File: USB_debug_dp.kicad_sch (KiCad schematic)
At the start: 0 parts

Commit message: [#82055] Add DP port controller
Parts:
- added C1, C13, C34, C37, C5, C56, C6: C_10u_0402, antmicro-footprints:C_0402_1005Metric, symbol antmicroCapacitors0402:C_10u_0402
- added C10, C11, C12, C14, C140, C141, C143, C144, C15, C16, C2, C3, C35, C38, C39, C54, C55, C7, C9: C_100n_0402, antmicro-footprints:C_0402_1005Metric, symbol antmicroCapacitors0402:C_100n_0402
- added C33, C36: C_4u7_25V_0402, antmicro-footprints:C_0402_1005Metric, symbol antmicroCapacitors0402:C_4u7_25V_0402
- added C41, C42, C43, C44: C_100n_0201, antmicro-footprints:C_0201, symbol antmicroCapacitorsmisc:C_100n_0201
- added C8: C_10u_25V_0603, antmicro-footprints:C_0603_1608Metric, symbol antmicroCapacitors0603:C_10u_25V_0603
- added D1: RB521S30T1G, antmicro-footprints:SOD-523, symbol antmicroDiodesRectifiersSingle:RB521S30T1G
- added D2, D3, D4, D5: LED_G_0603_LTST-C190GKT, antmicro-footprints:LED_0603_1608Metric_G, symbol antmicroLEDIndicationDiscrete:LED_G_0603_LTST-C190GKT
- added J2: USB-C_Amphenol_12401598E4, antmicro-footprints:USB-C_Receptacle_Amphenol_12401598E4, symbol antmicroUSBConnectors:USB-C_Amphenol_12401598E4
- added J3: USB-C_GCT_USB4105-GF-A, antmicro-footprints:USB-C_Receptacle_GCT_USB4105-GF-A, symbol antmicroUSBConnectors:USB-C_GCT_USB4105-GF-A
- added Q1, Q2: PJE138K, antmicro-footprints:SOT-523, symbol antmicroTransistorsFETsMOSFETsSingle:PJE138K
- added R1, R205, R207, R7, R9: R_100k_0402, antmicro-footprints:R_0402_1005Metric, symbol antmicroResistors0402:R_100k_0402
- added R10, R30, R31, R32, R37, R38, R6, R8: R_10k_0402, antmicro-footprints:R_0402_1005Metric, symbol antmicroResistors0402:R_10k_0402
- added R109, R110: R_2M_0402, antmicro-footprints:R_0402_1005Metric, symbol antmicroResistors0402:R_2M_0402
- added R11, R12: R_1k_0402, antmicro-footprints:R_0402_1005Metric, symbol antmicroResistors0402:R_1k_0402
- added R13, R14, R20, R21: R_200R_0402, antmicro-footprints:R_0402_1005Metric, symbol antmicroResistors0402:R_200R_0402
- added R15: R_4x0R_0201_array, antmicro-footprints:R_Array_4x0201_Panasonic_EXB18V, symbol antmicroResistorNetworksArrays:R_4x0R_0201_array
- added R16, R17, R18, R19, R26, R27, R28, R29, R33, R34, R35, R36, R5, R75, R79, R82: R_0R_0402, antmicro-footprints:R_0402_1005Metric, symbol antmicroResistors0402:R_0R_0402
- added R2: R_10M_0402, antmicro-footprints:R_0402_1005Metric, symbol antmicroResistors0402:R_10M_0402
- added R22, R23, R24, R25: R_4k7_0402, antmicro-footprints:R_0402_1005Metric, symbol antmicroResistors0402:R_4k7_0402
- added R39, R40: R_2k2_0402, antmicro-footprints:R_0402_1005Metric, symbol antmicroResistors0402:R_2k2_0402
- added TP1, TP28, TP3, TP30, TP4, TP5, TP6, TP7, TP8: TP_0.75mm_SMD, antmicro-footprints:TP_SMD_0.75mm, symbol antmicroTestPoints:TP_0.75mm_SMD
- added U1: NTS0102_XSON, antmicro-footprints:XSON-8_1x1.95mm_P0.5mm, symbol antmicroLogicTranslatorsLevelShifters:NTS0102_XSON
- added U10: TUSB1046-DCIRNQ, antmicro-footprints:WQFN-40_1EP_6x3mm_Pitch0.4mm_EP4.7x2.7mm, symbol antmicroInterfaceControllers:TUSB1046-DCIRNQ
- added U2: W25Q80DV_USON, antmicro-footprints:USON-8_2x3mm_P0.5mm, symbol antmicroMemory:W25Q80DV_USON
- added U3: TPS65988DHRSHR, antmicro-footprints:IC_TPS65987DDHRSHR, symbol antmicroInterfaceControllers:TPS65988DHRSHR
- added U4: NCP730BMT330_WSON, antmicro-footprints:WSON-6-1EP_2x2mm_P0.65mm, symbol antmicroPMICVoltageRegulatorsLinear:NCP730BMT330_WSON
- added U5: FT230X_QFN, antmicro-footprints:QFN-16-1EP_4x4mm_P0.65mm, symbol antmicroInterfaceControllers:FT230X_QFN
- added U6, U7: AP22615A_TSOT26, antmicro-footprints:TSOT23-6, symbol antmicroPMICPowerDistributionSwitchesLoadDrivers:AP22615A_TSOT26
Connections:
- new net: TP28.1, U10.29 (CAD_SNK/RSVD1)
- new net: C43.1, J2.B2 (TX_{2}+)
- new net: D2.2 (A), R13.1
- new net: C10.1, R30.2, U5.9 (~{RESET})
- new net: D5.2 (A), R21.2
- new net: D4.2 (A), R20.2
- new net: R34.2, R37.2, U6.4 (EN)
- new net: Q2.1 (G), R2.2
- new net: J2.A4 (VBUS), J2.A9 (VBUS), J2.B4 (VBUS), J2.B9 (VBUS), U3.13 (VBUS1), U7.1 (OUT)
- new net: R36.2, R38.2, U7.4 (EN)
- new net: R40.2, U7.5 (ISET)
- new net: TP8.1, U3.30 (GPIO3/HPD1)
- new net: U3.15 (DRAIN1), U3.19 (DRAIN1), U3.58 (DRAIN1), U3.8 (DRAIN1)
- new net: J2.A5 (CC_{1}), U3.24 (C1_CC1)
- new net: J2.B5 (CC_{2}), U3.26 (C1_CC2)
- new net: R39.2, U6.5 (ISET)
- new net: C41.1, J2.A2 (TX_{1}+)
- new net: C42.1, J2.A3 (TX_{1}-)
- new net: C44.1, J2.B3 (TX_{2}-)
- new net: R29.2, U5.4 (~{CTS})
- new net: J3.A4 (VBUS), J3.A9 (VBUS), J3.B4 (VBUS), J3.B9 (VBUS), U3.3 (VBUS2), U6.1 (OUT)
- new net: J3.A5 (CC_{1}), U3.45 (C2_CC1)
- new net: J3.B5 (CC_{2}), U3.47 (C2_CC2)
- new net: R28.2, U5.16 (~{RTS})
- new net: R27.2, U5.2 (RXD)
- new net: R26.2, U5.15 (TXD)
- new net: D3.2 (A), R14.1
- new net: U3.52 (DRAIN2), U3.56 (DRAIN2), U3.57 (DRAIN2), U3.7 (DRAIN2)
- new net +3V3: C1.2, C2.1, C38.1, C39.1, C54.1, C55.1, C56.2, R207.2, R22.1, R23.1, R24.1, R25.1, R31.2, R32.2, U10.1 (VCC), U10.20 (VCC), U10.28 (VCC), U10.6 (VCC), U3.5 (VIN_3V3)
- new net +5V: C15.1, C34.1, C35.1, C37.1, R33.2, R35.2, U3.25 (PP1_CABLE), U3.46 (PP2_CABLE), U6.6 (IN), U7.6 (IN)
- new net DEBUG_RXD: R26.1
- new net DEBUG_TXD: R27.1
- new net DP1_AUX_N: R207.1, U10.25 (AUX_N)
- new net DP1_AUX_P: R205.1, U10.24 (AUX_P)
- new net DP1_TXD0_N: U10.10 (DP0_N)
- new net DP1_TXD0_P: U10.9 (DP0_P)
- new net DP1_TXD1_N: U10.13 (DP1_N)
- new net DP1_TXD1_P: U10.12 (DP1_P)
- new net DP1_TXD2_N: U10.16 (DP2_N)
- new net DP1_TXD2_P: U10.15 (DP2_P)
- new net DP1_TXD3_N: U10.19 (DP3_N)
- new net DP1_TXD3_P: U10.18 (DP3_P)
- new net EEPROM_PWR: C9.2, D1.1 (C), R10.2, U2.3 (~{WP}/IO2), U2.7 (~{HOLD}/IO3), U2.8 (VCC)
- new net FTDI_3V3: C11.1, C12.1, C13.2, C3.1, C7.1, R1.2, R11.2, R12.2, R13.2, R14.2, R30.1, U1.3 (VCC_{A}), U1.7 (VCC_{B}), U4.1 (V_{OUT}), U5.1 (V_{CCIO}), U5.10 (V_{CC}), U5.8 (3V3_{OUT})
- new net FTDI_CBUS0/SDA: R12.1, U1.5 (A_{1}), U5.12 (CBUS0)
- new net FTDI_CBUS3/SCL: R11.1, U1.4 (A_{2}), U5.14 (CBUS3)
- new net FTDI_CBUS_EN: Q1.3 (D), Q2.3 (D), R1.1, U1.6 (OE)
- new net FTDI_LED_RX: D3.1 (C), Q1.1 (G), U5.11 (CBUS1)
- new net FTDI_LED_TX: D2.1 (C), U5.5 (CBUS2)
- new net GND: C1.1, C10.2, C11.2, C12.2, C13.1, C14.2, C15.2, C16.2, C2.2, C3.2, C33.2, C34.2, C35.2, C36.2, C37.2, C38.2, C39.2, C5.1, C54.2, C55.2, C56.1, C6.1, C7.2, C8.2, C9.1, D4.1 (C), D5.1 (C), J2.A1 (GND), J2.A12 (GND), J2.B1 (GND), J2.B12 (GND), J2.SH, J3.A1 (GND), J3.A12 (GND), J3.B1 (GND), J3.B12 (GND), J3.SH, Q1.2 (S), Q2.2 (S), R109.2, R110.2, R2.1, R205.2, R37.1, R38.1, R39.1, R40.1, R5.1, R7.1, R9.1, U1.2 (GND), U2.4 (VSS), U3.20 (GND), U3.51 (GND), U3.59 (GND_EP), U4.3 (GND), U4.5 (PG), U4.7 (GND), U5.13 (GND), U5.17 (GND), U5.3 (GND), U6.2 (GND), U7.2 (GND)
- new net GPIO010: R17.1
- new net HPDIN: R75.2, U10.32 (HPDIN/RSVD2)
- new net PDC_ADCIN1: R6.2, R7.2, U3.6 (ADCIN1)
- new net PDC_ADCIN2: R8.2, R9.2, U3.10 (ADCIN2)
- new net PDC_CTL0: R15.2 (R2.1), U3.17 (GPIO1)
- new net PDC_CTL1: R15.1 (R1.1), U3.18 (GPIO2)
- new net PDC_FLIP: R15.3 (R3.1), U3.16 (GPIO0)
- new net PDC_GPIO14: R20.1, U3.42 (GPIO14/PWM1)
- new net PDC_GPIO15: R21.1, U3.43 (GPIO15/PWM2)
- new net PDC_HPD2: R16.2, U3.31 (GPIO4/HPD2)
- new net PDC_I2C1_IRQn: R17.2, U3.29 (~{I2C1_IRQ})
- new net PDC_I2C1_SCL: R18.2, R23.2, U3.27 (I2C1_SCL)
- new net PDC_I2C1_SDA: R19.2, R22.2, U3.28 (I2C1_SDA)
- new net PDC_I2C2_IRQn: TP1.1, U3.34 (~{I2C2_IRQ})
- new net PDC_I2C2_SCL: R25.2, TP3.1, U3.32 (I2C2_SCL)
- new net PDC_I2C2_SDA: R24.2, TP4.1, U3.33 (I2C2_SDA)
- new net PDC_I2C3_SCL: TP5.1, U3.21 (I2C3_SCL/GPIO5)
- new net PDC_I2C3_SDA: TP6.1, U3.22 (I2C3_SDA/GPIO6)
- new net PDC_LDO_1V8: C5.2, U3.35 (LDO_1V8)
- new net PDC_LDO_3V3: C6.2, D1.2 (A), R6.1, R8.1, U3.9 (LDO_3V3)
- new net PDC_MISO: R10.1, U2.2 (SO/IO1), U3.36 (SPI_POCI/GPIO8)
- new net PDC_MOSI: U2.5 (SI/IO0), U3.37 (SPI_PICO/GPIO9)
- new net PDC_RESET: R5.2, U3.44 (HRESET)
- new net PDC_SCLK: U2.6 (SCLK), U3.38 (SPI_CLK/GPIO10)
- new net PWR_SOFT: R28.1
- new net SYS_CLK: R18.1, U1.1 (B_{2})
- new net SYS_SCL: R82.2
- new net SYS_SDA: R19.1, R79.2, U1.8 (B_{1})
- new net USBC0_5V_PEN: R35.1, R36.1, U3.48 (GPIO16/PP_EXT1)
- new net USBC0_CTL0: R15.7 (R2.2), R79.1, U10.22 (CTL0/SDA)
- new net USBC0_CTL1: R15.8 (R1.2), U10.23 (CTL1/HPDIN)
- new net USBC0_DPEQ0: U10.14 (DPEQ0/A1)
- new net USBC0_DPEQ1: U10.2 (DPEQ1)
- new net USBC0_EQ0: U10.38 (EQ0)
- new net USBC0_EQ1: U10.35 (EQ1)
- new net USBC0_FLG: R32.1, U7.3 (FLG)
- new net USBC0_FLIP: R15.6 (R3.2), R82.1, U10.21 (FLIP/SCL)
- new net USBC0_I2C_EN: U10.17 (I2C_EN)
- new net USBC0_RX1_N: J2.B10 (RX_{1}-), U10.31 (RX1_N)
- new net USBC0_RX1_P: J2.B11 (RX_{1}+), U10.30 (RX1_P)
- new net USBC0_RX2_N: J2.A10 (RX_{2}-), U10.39 (RX2_N)
- new net USBC0_RX2_P: J2.A11 (RX_{2}+), U10.40 (RX2_P)
- new net USBC0_SBU_N: J2.A8 (SBU_{1}), R109.1, U10.27 (SBU1)
- new net USBC0_SBU_P: J2.B8 (SBU_{2}), R110.1, U10.26 (SBU2)
- new net USBC0_SSEQ0: U10.11 (SSEQ0/A0)
- new net USBC0_SSEQ1: U10.3 (SSEQ1)
- new net USBC0_TX1_N: C42.2, U10.34 (TX1_N)
- new net USBC0_TX1_P: C41.2, U10.33 (TX1_P)
- new net USBC0_TX2_N: C44.2, U10.36 (TX2_N)
- new net USBC0_TX2_P: C43.2, U10.37 (TX2_P)
- new net USBC1_5V_PEN: R33.1, R34.1, U3.49 (GPIO17/PP_EXT2)
- new net USBC1_FLG: R31.1, U6.3 (FLG)
- new net USBC3_VBUS: C8.1, U4.4 (EN), U4.6 (V_{IN})
- new net USBC_HPD: R16.1, R75.1, TP30.1
- new net USBPD0_HV: C16.1, C36.1, U3.11 (PP_HV1)
- new net USBPD1_HV: C14.1, C33.1, U3.1 (PP_HV2)
- new net USBSS0_RX_C_N: C140.2, U10.4 (SSRX_N)
- new net USBSS0_RX_C_P: C143.2, U10.5 (SSRX_P)
- new net USBSS0_RX_N: C143.1
- new net USBSS0_RX_P: C140.1
- new net USBSS0_TX_C_N: C141.2, U10.7 (SSTX_N)
- new net USBSS0_TX_C_P: C144.2, U10.8 (SSTX_P)
- new net USBSS0_TX_N: C144.1
- new net USBSS0_TX_P: C141.1
- new net USB_FTDI_N: J3.A7 (D_{A}-), J3.B7 (D_{B}-), U5.7 (D-)
- new net USB_FTDI_P: J3.A6 (D_{A}+), J3.B6 (D_{B}+), U5.6 (D+)
- new net ~{PDC_CS}: U2.1 (~{CS}), U3.39 (~{SPI_CS}/GPIO11)
- new net ~{PDC_I2C3_IRQ}: TP7.1, U3.23 (~{I2C3_IRQ}/GPIO7)
- no-connect marks 0 -> 14
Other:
- note added: "4 LANE DP"
- note added: "CONFIGURATION"
- note added: "CTL0"
- note added: "CTL1"
- note added: "H"
- note added: "I_{LIM}(A) = 6800/R_{LIM} = 3.09"
- note added: "L"
- note added: "POWER DOWN"
- note added: "RX"
- note added: "TX"
- note added: "USB + 2 LANE DP"
- note added: "USB ONLY"
- note added: "USB PORT 0"
- note added: "USB PORT 1"

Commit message: [#82055] Add DP eq connections, cleanup schematic
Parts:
- removed C35: C_100n_0402, antmicro-footprints:C_0402_1005Metric, symbol antmicroCapacitors0402:C_100n_0402
- removed D1: RB521S30T1G, antmicro-footprints:SOD-523, symbol antmicroDiodesRectifiersSingle:RB521S30T1G
- removed J3: USB-C_GCT_USB4105-GF-A, antmicro-footprints:USB-C_Receptacle_GCT_USB4105-GF-A, symbol antmicroUSBConnectors:USB-C_GCT_USB4105-GF-A
- removed Q1: PJE138K, antmicro-footprints:SOT-523, symbol antmicroTransistorsFETsMOSFETsSingle:PJE138K
- removed R1, R7, R9: R_100k_0402, antmicro-footprints:R_0402_1005Metric, symbol antmicroResistors0402:R_100k_0402
- removed R10: R_10k_0402, antmicro-footprints:R_0402_1005Metric, symbol antmicroResistors0402:R_10k_0402
- removed R12: R_1k_0402, antmicro-footprints:R_0402_1005Metric, symbol antmicroResistors0402:R_1k_0402
- removed R17, R19, R5, R75, R82: R_0R_0402, antmicro-footprints:R_0402_1005Metric, symbol antmicroResistors0402:R_0R_0402
- removed R22, R25: R_4k7_0402, antmicro-footprints:R_0402_1005Metric, symbol antmicroResistors0402:R_4k7_0402
- removed TP1: TP_0.75mm_SMD, antmicro-footprints:TP_SMD_0.75mm, symbol antmicroTestPoints:TP_0.75mm_SMD
- removed U3: TPS65988DHRSHR, antmicro-footprints:IC_TPS65987DDHRSHR, symbol antmicroInterfaceControllers:TPS65988DHRSHR
- added C145, C146: C_47p_0402, antmicro-footprints:C_0402_1005Metric, symbol antmicroCapacitors0402:C_47p_0402
- added C147: C_1u_25V_0402, antmicro-footprints:C_0402_1005Metric, symbol antmicroCapacitors0402:C_1u_25V_0402
- added C40, C93: C_100n_0402, antmicro-footprints:C_0402_1005Metric, symbol antmicroCapacitors0402:C_100n_0402
- added D19: DF2S30FS_SOD, antmicro-footprints:SOD-923, symbol antmicroTVSDiodes:DF2S30FS_SOD
- added D20: LED_G_0603_LTST-C190GKT, antmicro-footprints:LED_0603_1608Metric_G, symbol antmicroLEDIndicationDiscrete:LED_G_0603_LTST-C190GKT
- added D6: RB521S30T1G, antmicro-footprints:SOD-523, symbol antmicroDiodesRectifiersSingle:RB521S30T1G
- added J4: USB-C_GCT_USB4105-GF-A, antmicro-footprints:USB-C_Receptacle_GCT_USB4105-GF-A, symbol antmicroUSBConnectors:USB-C_GCT_USB4105-GF-A
- added Q3: PJE138K, antmicro-footprints:SOT-523, symbol antmicroTransistorsFETsMOSFETsSingle:PJE138K
- added R100, R101, R102, R103, R104, R105, R106, R107, R108, R111, R113, R63, R67, R68, R70: R_1k_0402, antmicro-footprints:R_0402_1005Metric, symbol antmicroResistors0402:R_1k_0402
- added R117, R127: R_27R_0402, antmicro-footprints:R_0402_1005Metric, symbol antmicroResistors0402:R_27R_0402
- added R41, R56, R58, R61, R65: R_0R_0402, antmicro-footprints:R_0402_1005Metric, symbol antmicroResistors0402:R_0R_0402
- added R42, R43, R54: R_100k_0402, antmicro-footprints:R_0402_1005Metric, symbol antmicroResistors0402:R_100k_0402
- added R48: R_10k_0402, antmicro-footprints:R_0402_1005Metric, symbol antmicroResistors0402:R_10k_0402
- added R50, R52, R71: R_4k7_0402, antmicro-footprints:R_0402_1005Metric, symbol antmicroResistors0402:R_4k7_0402
- added TP9: TP_0.75mm_SMD, antmicro-footprints:TP_SMD_0.75mm, symbol antmicroTestPoints:TP_0.75mm_SMD
- added U17, U18, U19, U20: TPD4E05U06QDQARQ1, antmicro-footprints:USON-10_2.5x1mm_P0.5mm, symbol antmicroTVSDiodes:TPD4E05U06QDQARQ1
- added U8: TPS65988DHRSHR, antmicro-footprints:IC_TPS65987DDHRSHR, symbol antmicroInterfaceControllers:TPS65988DHRSHR
- renumbered C1 to C60, C2 to C61, C5 to C62, C6 to C63, C9 to C64, C8 to C65, C56 to C66, C38 to C67, C39 to C68, C143 to C69, C144 to C70, C140 to C71, C141 to C72, C54 to C73, C55 to C74, C11 to C75, C12 to C76, C13 to C77, C3 to C78, C7 to C79, C10 to C80, C41 to C81, C43 to C82, C16 to C83, C14 to C84, C42 to C86, C44 to C87, C15 to C88, C36 to C89, C37 to C90, C33 to C91, C34 to C92, D4 to D15, D5 to D16, D2 to D17, D3 to D18, J2 to J4, Q2 to Q15, R6 to R56, R8 to R58, R15 to R61, R16 to R63, R18 to R65, R20 to R67, R21 to R68, R23 to R70, R24 to R71, R2 to R73, R11 to R74, R207 to R76, R205 to R77, R13 to R78, R14 to R80, R79 to R81, R26 to R83, R27 to R84, R28 to R85, R29 to R86, R32 to R87, R31 to R88, R30 to R89, R35 to R90, R33 to R91, R36 to R92, R34 to R93, R38 to R94, R37 to R95, R40 to R96, R39 to R97, R109 to R98, R110 to R99, TP4 to TP10, TP5 to TP11, TP6 to TP12, TP7 to TP13, TP8 to TP14, TP30 to TP15, TP28 to TP16, TP3 to TP9, U4 to U11, U1 to U12, U10 to U13, U5 to U14, U7 to U15, U6 to U16, U2 to U9
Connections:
- net +3V3: now also R100.2, R102.2, R104.2, R106.2, R108.2, R50.1, R52.1, R68.2, R70.2, U8.5 (VIN_3V3)
- net +5V: now also C40.1, U8.25 (PP1_CABLE), U8.46 (PP2_CABLE)
- net EEPROM_PWR: now also D6.1 (C), R48.2
- net FTDI_3V3: now also R54.2, R63.2
- net FTDI_CBUS0/SDA: now also R63.1
- net FTDI_CBUS_EN: now also Q3.3 (D), R54.1
- net FTDI_LED_RX: now also Q3.1 (G)
- net GND: now also U13.41 (GND), C145.1, C146.2, C147.2, C40.2, C93.2, D19.2 (A), D20.1 (C), J4.A1 (GND), J4.A12 (GND), J4.B1 (GND), J4.B12 (GND), J4.SH, Q3.2 (S), R101.2, R103.2, R105.2, R107.2, R111.2, R113.2, R41.1, R42.1, R43.1, R67.2, U17.3, U17.8, U18.3, U18.8, U19.3, U19.8, U20.3, U20.8, U8.20 (GND), U8.51 (GND), U8.59 (GND_EP)
- net GPIO010: now also R56.1
- net HPDIN: now also R61.2
- net PDC_ADCIN1: now also R42.2, U8.6 (ADCIN1)
- net PDC_ADCIN2: now also R43.2, U8.10 (ADCIN2)
- net PDC_CTL0: now also U8.17 (GPIO1)
- net PDC_CTL1: now also U8.18 (GPIO2)
- net PDC_FLIP: now also U8.16 (GPIO0)
- net PDC_GPIO14: now also U8.42 (GPIO14/PWM1)
- net PDC_GPIO15: now also U8.43 (GPIO15/PWM2)
- net PDC_HPD2: now also U8.31 (GPIO4/HPD2)
- net PDC_I2C1_IRQn: now also R56.2, U8.29 (~{I2C1_IRQ})
- net PDC_I2C1_SCL: now also R50.2, U8.27 (I2C1_SCL); no longer R70.2
- net PDC_I2C1_SDA: now also R70.2, R58.2, U8.28 (I2C1_SDA)
- net PDC_I2C2_IRQn: now also TP9.1, U8.34 (~{I2C2_IRQ})
- net PDC_I2C2_SCL: now also R71.2, U8.32 (I2C2_SCL)
- net PDC_I2C2_SDA: now also R52.2, U8.33 (I2C2_SDA); no longer R71.2
- net PDC_I2C3_SCL: now also U8.21 (I2C3_SCL/GPIO5)
- net PDC_I2C3_SDA: now also U8.22 (I2C3_SDA/GPIO6)
- net PDC_LDO_1V8: now also U8.35 (LDO_1V8)
- net PDC_LDO_3V3: now also D6.2 (A), U8.9 (LDO_3V3)
- net PDC_MISO: now also R48.1, U8.36 (SPI_POCI/GPIO8)
- net PDC_MOSI: now also U8.37 (SPI_PICO/GPIO9)
- net PDC_RESET: now also R41.2, U8.44 (HRESET)
- net PDC_SCLK: now also U8.38 (SPI_CLK/GPIO10)
- net SYS_SCL: now also R65.2
- net SYS_SDA: now also R58.1
- net USBC0_5V_PEN: now also U8.48 (GPIO16/PP_EXT1)
- net USBC0_FLIP: now also R65.1
- net USBC0_RX1_N: now also U20.5, U20.6
- net USBC0_RX1_P: now also U20.4, U20.7
- net USBC0_RX2_N: now also U19.5, U19.6
- net USBC0_RX2_P: now also U19.4, U19.7
- net USBC0_SBU_N: now also U18.4, U18.7
- net USBC0_SBU_P: now also U18.5, U18.6
- net USBC1_5V_PEN: now also U8.49 (GPIO17/PP_EXT2)
- net USBC_HPD: now also R61.1
- net USBPD0_HV: now also U8.11 (PP_HV1)
- net USBPD1_HV: now also U8.1 (PP_HV2)
- net USB_FTDI_N: now also R117.1
- net USB_FTDI_P: now also R127.1
- net ~{PDC_CS}: now also U8.39 (~{SPI_CS}/GPIO11)
- net ~{PDC_I2C3_IRQ}: now also U8.23 (~{I2C3_IRQ}/GPIO7)
- net at C82.1, J4.B2 (TX_{2}+): now also U18.1, U18.10
- net ~{PERIPHERAL_RESET}: now reaches Q15.1 (G), R73.2
- net at J4.A4 (VBUS), J4.A9 (VBUS), J4.B4 (VBUS)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: now also U8.13 (VBUS1)
- net at TP14.1: now also U8.30 (GPIO3/HPD1)
- net at J4.A5 (CC_{1}): now also U17.5, U17.6, U8.24 (C1_CC1)
- net at J4.B5 (CC_{2}): now also U17.4, U17.7, U8.26 (C1_CC2)
- net at C81.1, J4.A2 (TX_{1}+): now also U19.1, U19.10
- net at C86.1, J4.A3 (TX_{1}-): now also U19.2, U19.9
- net USB0_D+: now reaches J4.A6 (D_{A}+)
- net USB0_D+: now also J4.B6 (D_{B}+), U17.2, U17.9
- net USB0_D-: now reaches J4.A7 (D_{A}-)
- net USB0_D-: now also J4.B7 (D_{B}-), U17.1, U17.10
- net at C87.1, J4.B3 (TX_{2}-): now also U18.2, U18.9
- net at U16.1 (OUT): now also C147.1, C93.1, D19.1 (C), J4.A4 (VBUS), J4.A9 (VBUS), J4.B4 (VBUS), J4.B9 (VBUS), R71.1, U8.3 (VBUS2)
- net USBC0_DPEQ0: no longer names the net of U13.14 (DPEQ0/A1)
- net USBC0_DPEQ0: now also R106.1, R107.1
- net USBC0_DPEQ1: no longer names the net of U13.2 (DPEQ1)
- net USBC0_DPEQ1: now also R108.1, R67.1
- net USBC0_EQ0: no longer names the net of U13.38 (EQ0)
- net USBC0_EQ0: now also R111.1, R68.1
- net USBC0_EQ1: no longer names the net of U13.35 (EQ1)
- net USBC0_EQ1: now also R113.1, R70.1
- net USBC0_I2C_EN: no longer names the net of U13.17 (I2C_EN)
- net USBC0_I2C_EN: now also R100.1, R101.1
- net USBC0_SSEQ0: no longer names the net of U13.11 (SSEQ0/A0)
- net USBC0_SSEQ0: now also R102.1, R103.1
- net USBC0_SSEQ1: no longer names the net of U13.3 (SSEQ1)
- net USBC0_SSEQ1: now also R104.1, R105.1
- new net: C145.2, J4.A7 (D_{A}-), J4.B7 (D_{B}-), R117.2
- new net: C146.1, J4.A6 (D_{A}+), J4.B6 (D_{B}+), R127.2
- new net: D20.2 (A), R71.2
- new net: U20.1, U20.10
- new net: U20.2, U20.9
- new net: U8.15 (DRAIN1), U8.19 (DRAIN1), U8.58 (DRAIN1), U8.8 (DRAIN1)
- new net: J4.A5 (CC_{1}), U8.45 (C2_CC1)
- new net: J4.B5 (CC_{2}), U8.47 (C2_CC2)
- new net: U8.52 (DRAIN2), U8.56 (DRAIN2), U8.57 (DRAIN2), U8.7 (DRAIN2)
- no-connect marks 14 -> 16
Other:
- moved on the sheet: C60, C61, C62, C63, C64, C65, C66, C67, C68, C69, C70, C71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

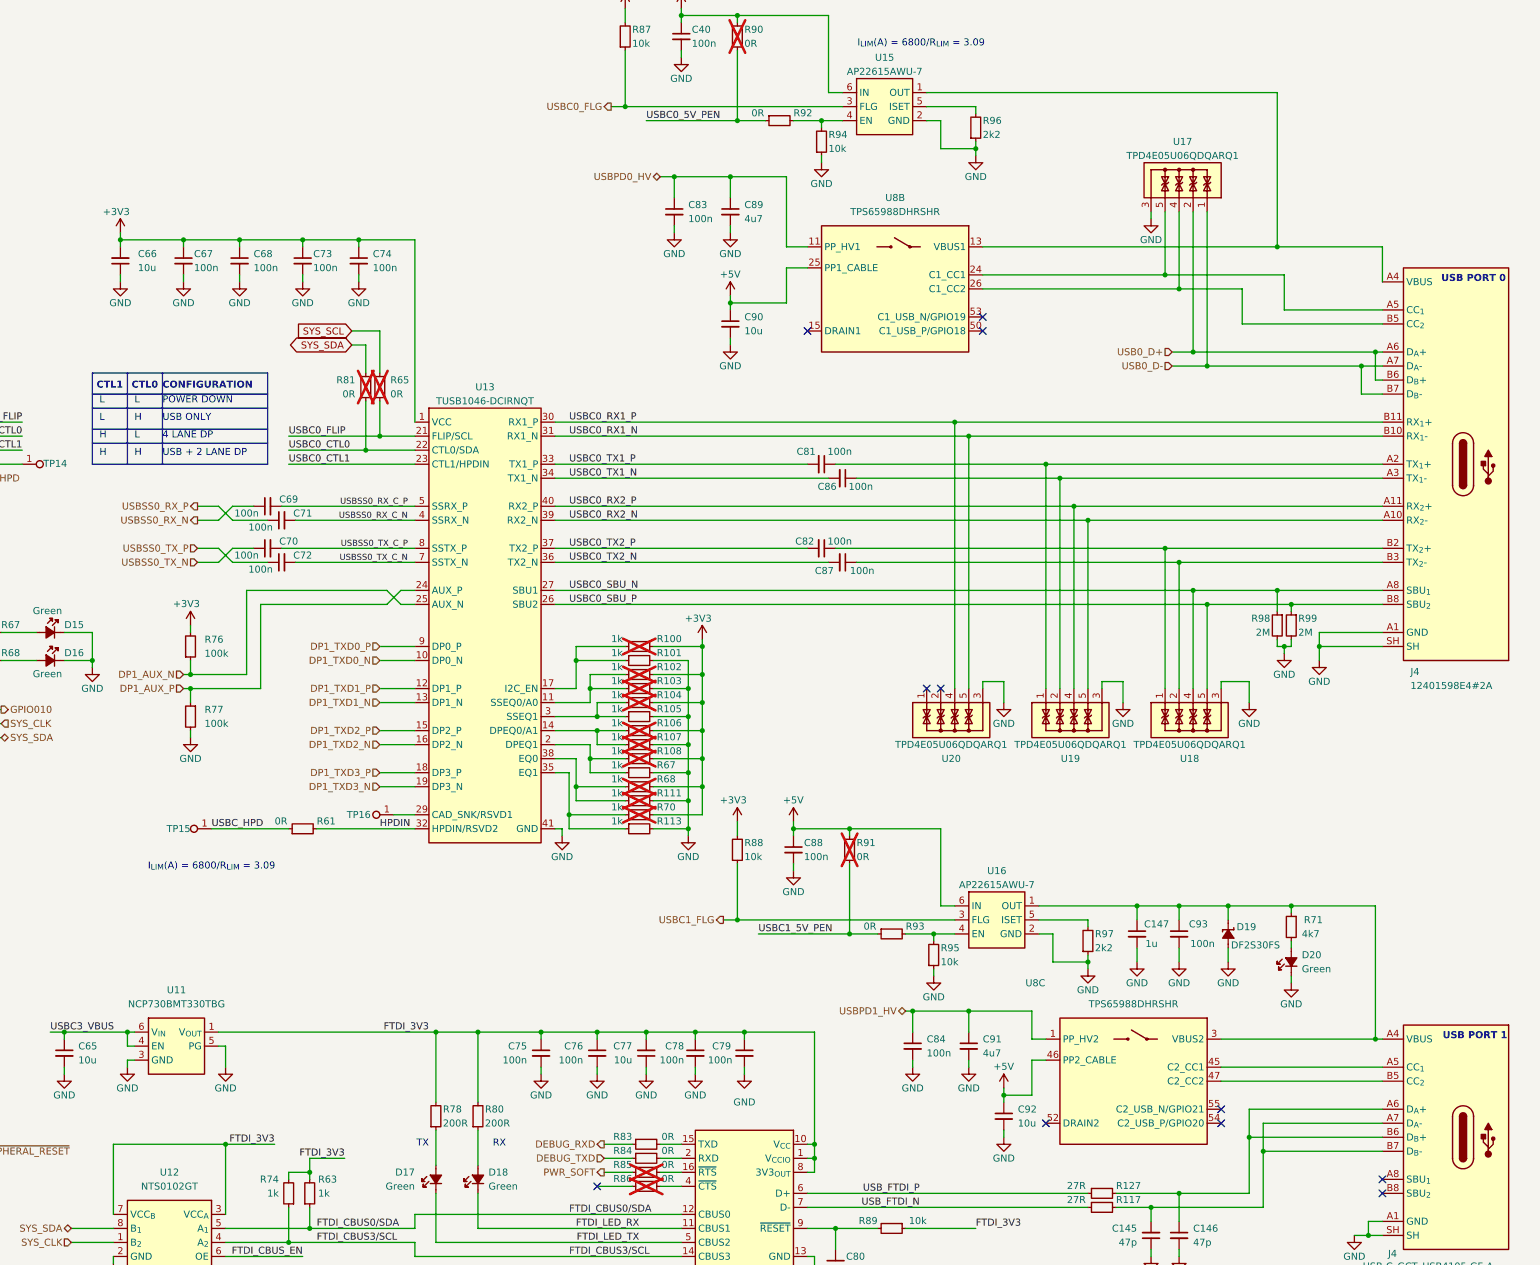
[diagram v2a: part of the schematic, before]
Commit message: [#82055] Add USB recovery port
[#81970] add discharge circuit

[#81970] Annotation

[#81782] Annotation and clean up
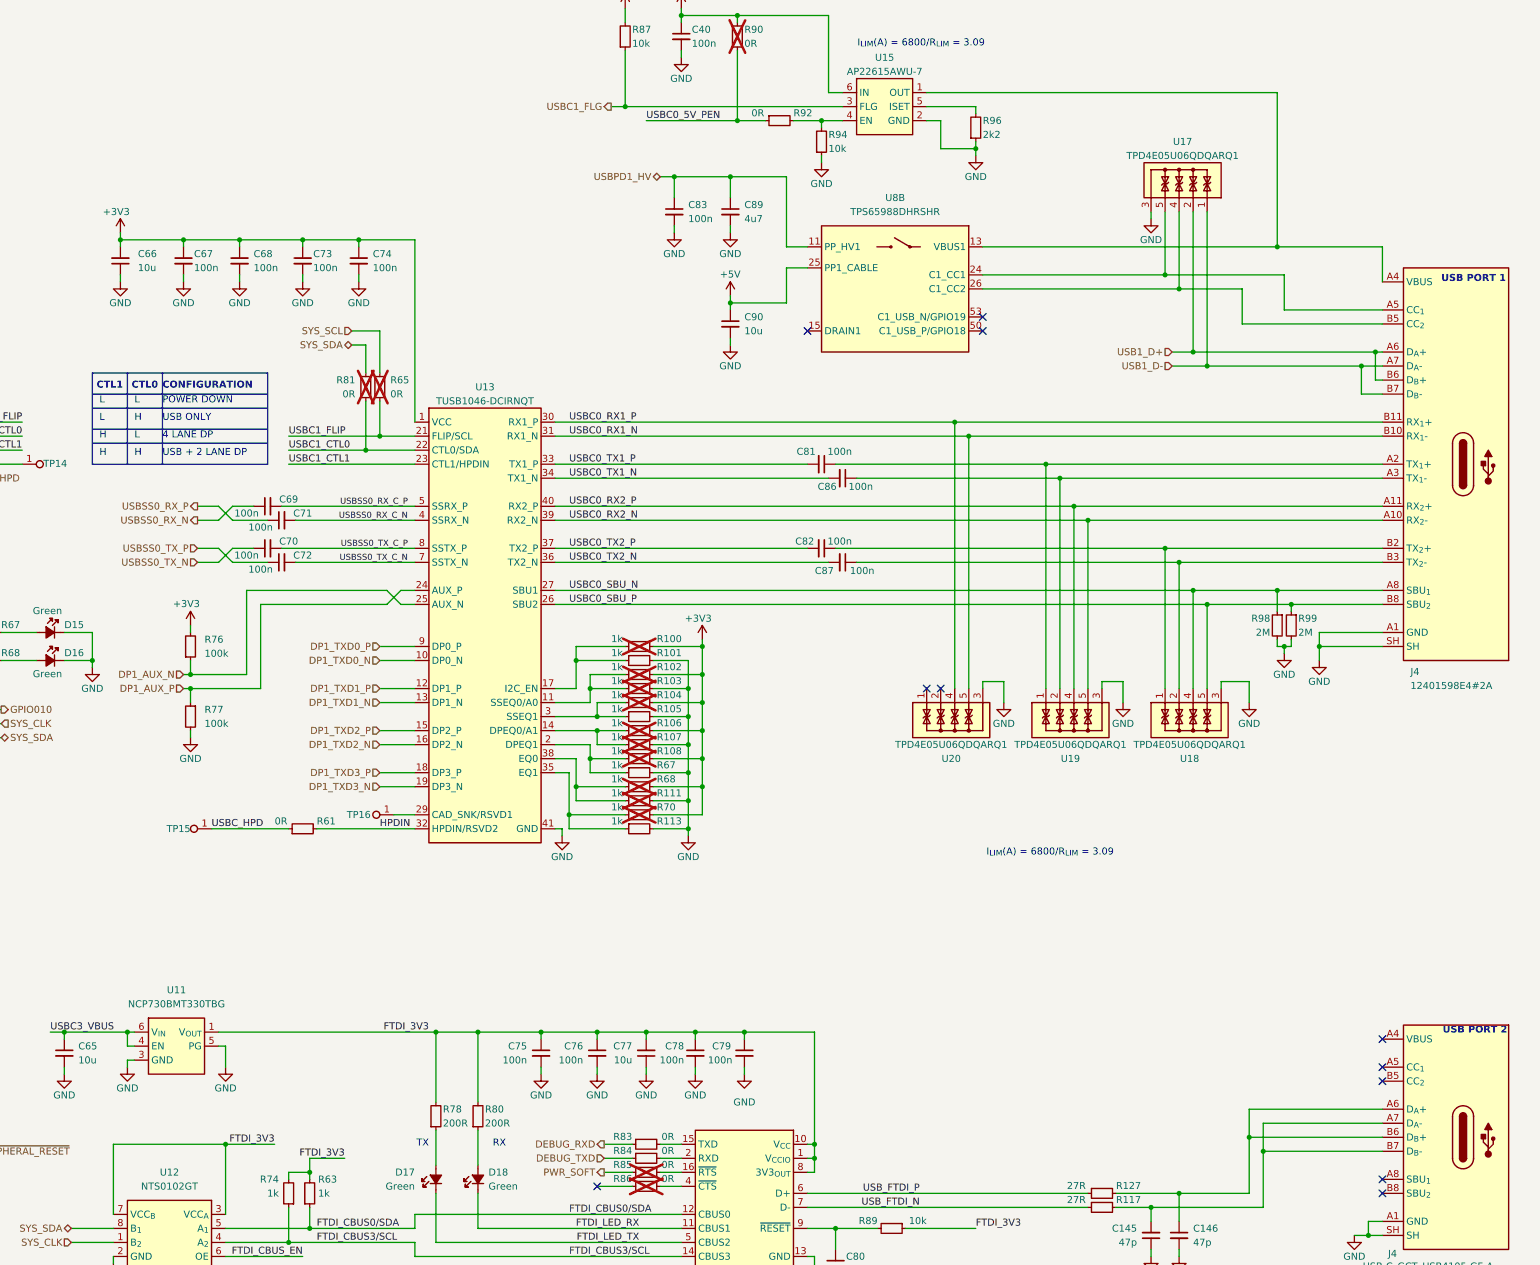
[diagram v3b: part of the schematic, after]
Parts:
- removed C147: C_1u_25V_0402, antmicro-footprints:C_0402_1005Metric, symbol antmicroCapacitors0402:C_1u_25V_0402
- removed C84, C88, C93: C_100n_0402, antmicro-footprints:C_0402_1005Metric, symbol antmicroCapacitors0402:C_100n_0402
- removed C91: C_4u7_25V_0402, antmicro-footprints:C_0402_1005Metric, symbol antmicroCapacitors0402:C_4u7_25V_0402
- removed C92: C_10u_0402, antmicro-footprints:C_0402_1005Metric, symbol antmicroCapacitors0402:C_10u_0402
- removed D19: DF2S30FS_SOD, antmicro-footprints:SOD-923, symbol antmicroTVSDiodes:DF2S30FS_SOD
- removed D20: LED_G_0603_LTST-C190GKT, antmicro-footprints:LED_0603_1608Metric_G, symbol antmicroLEDIndicationDiscrete:LED_G_0603_LTST-C190GKT
- removed R71: R_4k7_0402, antmicro-footprints:R_0402_1005Metric, symbol antmicroResistors0402:R_4k7_0402
- removed R88, R95: R_10k_0402, antmicro-footprints:R_0402_1005Metric, symbol antmicroResistors0402:R_10k_0402
- removed R91, R93: R_0R_0402, antmicro-footprints:R_0402_1005Metric, symbol antmicroResistors0402:R_0R_0402
- removed R97: R_2k2_0402, antmicro-footprints:R_0402_1005Metric, symbol antmicroResistors0402:R_2k2_0402
- removed U16: AP22615A_TSOT26, antmicro-footprints:TSOT23-6, symbol antmicroPMICPowerDistributionSwitchesLoadDrivers:AP22615A_TSOT26
- removed unit 3 of U8
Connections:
- net USBC0_FLG is gone; now on net USBC1_FLG: R87.1, U15.3 (FLG)
- net USBPD0_HV is gone; now on net USBPD1_HV: C83.1, C89.1, U8.11 (PP_HV1)
- net USBC0_CTL0: no longer R81.1, U13.22 (CTL0/SDA)
- net USBC0_CTL1: no longer U13.23 (CTL1/HPDIN)
- net USBC0_FLIP: no longer R65.1, U13.21 (FLIP/SCL)
- net USB0_D+ renamed USB1_D+
- net USB0_D- renamed USB1_D-
- new net USBC1_CTL0: R81.1, U13.22 (CTL0/SDA)
- new net USBC1_CTL1: U13.23 (CTL1/HPDIN)
- new net USBC1_FLIP: R65.1, U13.21 (FLIP/SCL)
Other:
- note added: "USB PORT 2"
- note removed: "USB PORT 0"
